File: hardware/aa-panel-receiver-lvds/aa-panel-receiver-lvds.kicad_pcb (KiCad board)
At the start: 2 copper layers, 95.4 x 54 mm, 44 parts, among them CN101 Conn_01x02, CN201 8P8C, CN202 Conn_01x08, CN251 Conn_01x04, U201 MC3486N, U202 Si8640EB-B-IU, U4 CRE1S0505S3C

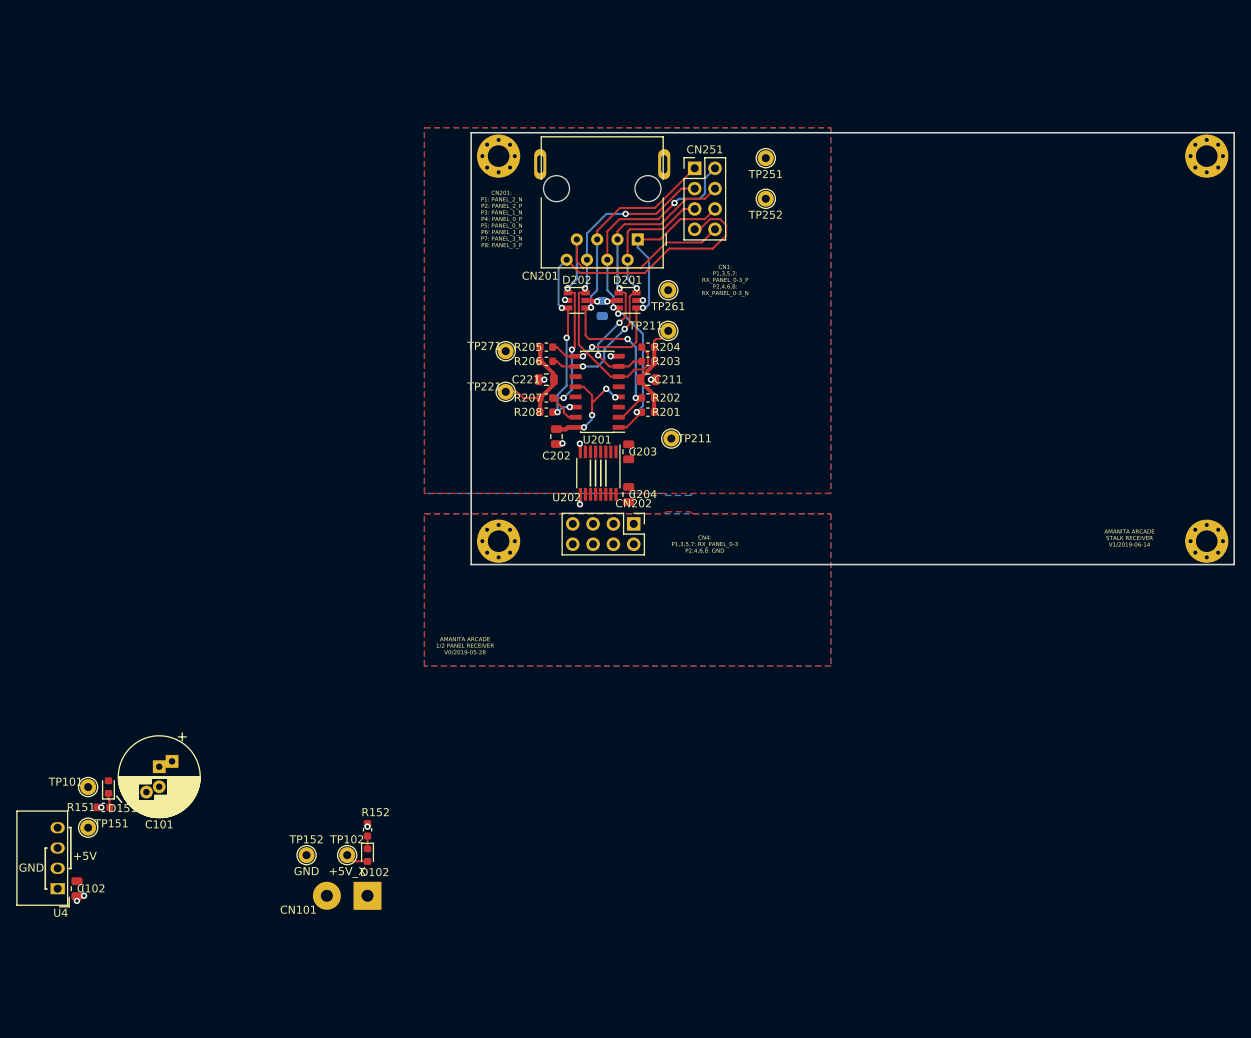
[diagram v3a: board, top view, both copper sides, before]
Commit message: Renumber and duplicate layout for panel receiver -- layout not complete
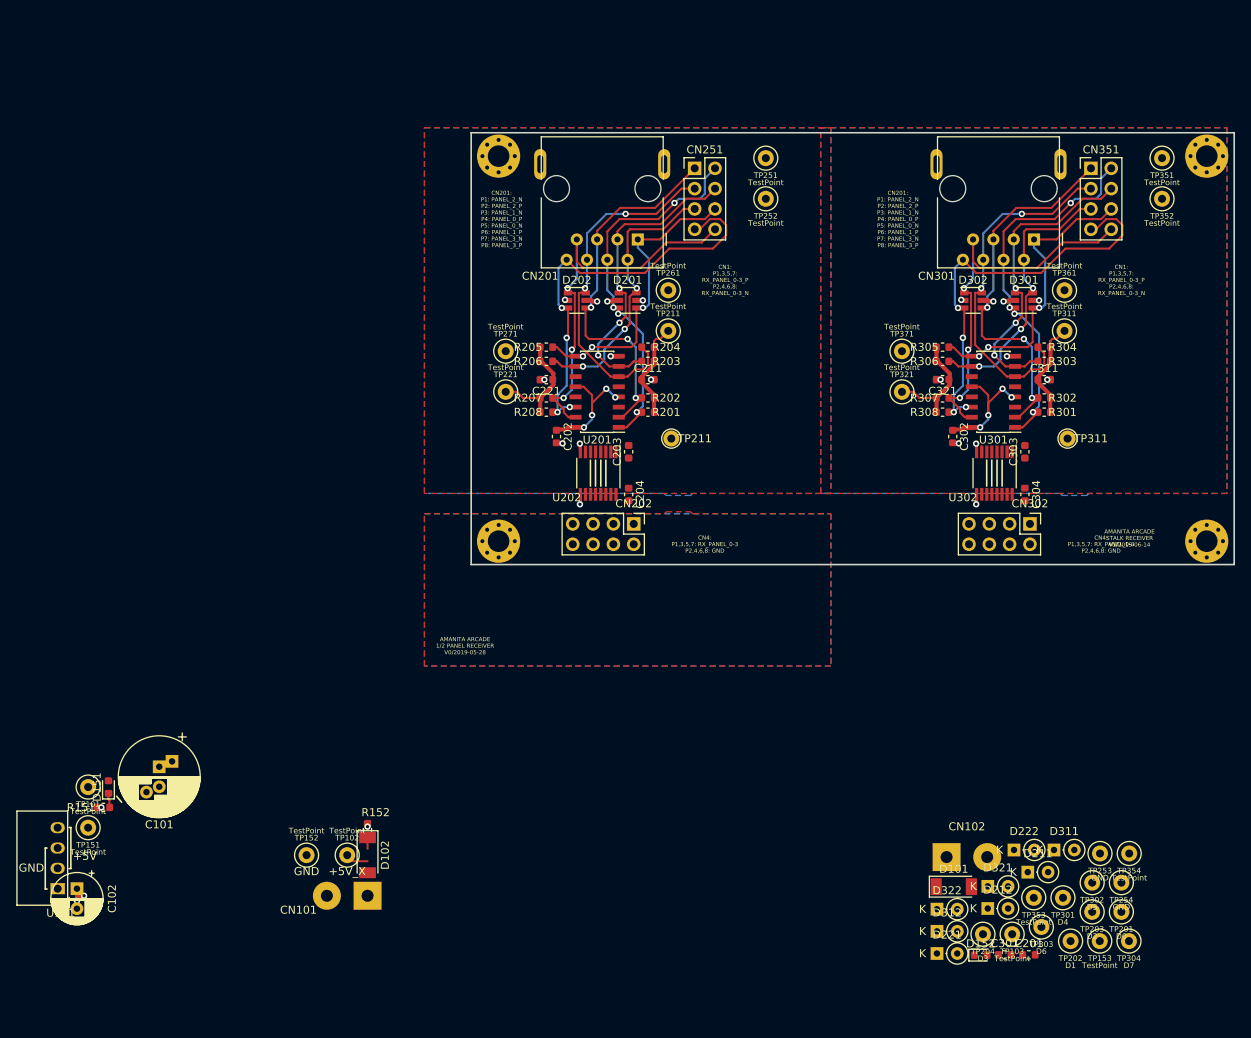
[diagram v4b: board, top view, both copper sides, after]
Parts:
- removed C1: 1u, Capacitor_SMD:C_0805_2012Metric
- added C201: 1u, Capacitor_SMD:C_0603_1608Metric, F.Cu at (161.2, 152.9)
- added C301: 1u, Capacitor_SMD:C_0603_1608Metric, F.Cu at (158.1, 152.9)
- added C302: 0.1u, Capacitor_SMD:C_0603_1608Metric, F.Cu at (151.6, 88.1)
- added C303: 0.1u, Capacitor_SMD:C_0603_1608Metric, F.Cu at (160.7, 90.0)
- added C304: 0.1u, Capacitor_SMD:C_0603_1608Metric, F.Cu at (160.7, 95.4)
- added C311: 0.1u, Capacitor_SMD:C_0603_1608Metric, F.Cu at (163.1, 81.0)
- added C321: 0.1u, Capacitor_SMD:C_0603_1608Metric, F.Cu at (150.4, 81.0)
- added CN102: Conn_01x02, Connector_Wire:SolderWirePad_1x02_P5.08mm_Drill1.5mm, F.Cu at (150.9, 140.7)
- added CN301: 8P8C, aa-shared:8P8C_Assmann_A-2014-2S-4, F.Cu at (161.8, 63.5)
- added CN302: Conn_01x08, Connector_PinHeader_2.54mm:PinHeader_2x04_P2.54mm_Vertical, F.Cu at (161.3, 99.1)
- added CN351: Conn_01x08, Connector_PinHeader_2.54mm:PinHeader_2x04_P2.54mm_Vertical, F.Cu at (168.9, 54.6)
- added D101: TSS83L45, aa-shared:D_SOD-128, F.Cu at (151.8, 144.4)
- added D152: LED, LED_SMD:LED_0603_1608Metric, F.Cu at (155.1, 153.0)
- added D211: D_Zener, Diode_THT:D_DO-35_SOD27_P2.54mm_Vertical_KathodeUp, F.Cu at (161.0, 142.6)
- added D212: D_Zener, Diode_THT:D_DO-35_SOD27_P2.54mm_Vertical_KathodeUp, F.Cu at (156.0, 147.1)
- added D221: D_Zener, Diode_THT:D_DO-35_SOD27_P2.54mm_Vertical_KathodeUp, F.Cu at (149.7, 152.8)
- added D222: D_Zener, Diode_THT:D_DO-35_SOD27_P2.54mm_Vertical_KathodeUp, F.Cu at (159.3, 139.8)
- added D301: D5V0P4UR6SO, Package_TO_SOT_SMD:SOT-23-6, F.Cu at (160.5, 71.1)
- added D302: D5V0P4UR6SO, Package_TO_SOT_SMD:SOT-23-6, F.Cu at (154.2, 71.1)
- added D311: D_Zener, Diode_THT:D_DO-35_SOD27_P2.54mm_Vertical_KathodeUp, F.Cu at (164.3, 139.8)
- added D312: D_Zener, Diode_THT:D_DO-35_SOD27_P2.54mm_Vertical_KathodeUp, F.Cu at (149.7, 150.0)
- added D321: D_Zener, Diode_THT:D_DO-35_SOD27_P2.54mm_Vertical_KathodeUp, F.Cu at (156.0, 144.4)
- added D322: D_Zener, Diode_THT:D_DO-35_SOD27_P2.54mm_Vertical_KathodeUp, F.Cu at (149.7, 147.2)
- added R301: 56, Resistor_SMD:R_0603_1608Metric, F.Cu at (163.1, 85.1)
- added R302: 56, Resistor_SMD:R_0603_1608Metric, F.Cu at (163.1, 83.3)
- added R303: 56, Resistor_SMD:R_0603_1608Metric, F.Cu at (163.1, 78.7)
- added R304: 56, Resistor_SMD:R_0603_1608Metric, F.Cu at (163.1, 77.0)
- added R305: 56, Resistor_SMD:R_0603_1608Metric, F.Cu at (150.4, 77.0)
- added R306: 56, Resistor_SMD:R_0603_1608Metric, F.Cu at (150.4, 78.7)
- added R307: 56, Resistor_SMD:R_0603_1608Metric, F.Cu at (150.4, 83.3)
- added R308: 56, Resistor_SMD:R_0603_1608Metric, F.Cu at (150.4, 85.1)
- added TP103: TestPoint, aa-shared:TestPoint_Loop_D1.80mm_Drill1.0mm_Beaded, F.Cu at (159.1, 150.3)
- added TP153: TestPoint, aa-shared:TestPoint_Loop_D1.80mm_Drill1.0mm_Beaded, F.Cu at (170.0, 151.2)
- added TP201: D0, aa-shared:TestPoint_Loop_D1.80mm_Drill1.0mm_Beaded, F.Cu at (172.7, 147.6)
- added TP202: D1, aa-shared:TestPoint_Loop_D1.80mm_Drill1.0mm_Beaded, F.Cu at (166.4, 151.2)
- added TP203: D2, aa-shared:TestPoint_Loop_D1.80mm_Drill1.0mm_Beaded, F.Cu at (169.1, 147.6)
- added TP204: D3, aa-shared:TestPoint_Loop_D1.80mm_Drill1.0mm_Beaded, F.Cu at (155.4, 150.3)
- added TP253: GND, aa-shared:TestPoint_Loop_D1.80mm_Drill1.0mm_Beaded, F.Cu at (170.0, 140.3)
- added TP254: GND, aa-shared:TestPoint_Loop_D1.80mm_Drill1.0mm_Beaded, F.Cu at (172.7, 143.9)
- added TP301: D4, aa-shared:TestPoint_Loop_D1.80mm_Drill1.0mm_Beaded, F.Cu at (165.4, 145.8)
- added TP302: D5, aa-shared:TestPoint_Loop_D1.80mm_Drill1.0mm_Beaded, F.Cu at (169.1, 143.9)
- added TP303: D6, aa-shared:TestPoint_Loop_D1.80mm_Drill1.0mm_Beaded, F.Cu at (162.7, 149.4)
- added TP304: D7, aa-shared:TestPoint_Loop_D1.80mm_Drill1.0mm_Beaded, F.Cu at (173.7, 151.2)
- added TP311: TestPoint, aa-shared:TestPoint_Loop_D1.80mm_Drill1.0mm_Beaded, F.Cu at (165.6, 74.9)
- added TP311: TestPoint, TestPoint:TestPoint_THTPad_D2.0mm_Drill1.0mm, F.Cu at (166.0, 88.4)
- added TP321: TestPoint, aa-shared:TestPoint_Loop_D1.80mm_Drill1.0mm_Beaded, F.Cu at (145.3, 82.5)
- added TP351: TestPoint, aa-shared:TestPoint_Loop_D1.80mm_Drill1.0mm_Beaded, F.Cu at (177.8, 53.3)
- added TP352: TestPoint, aa-shared:TestPoint_Loop_D1.80mm_Drill1.0mm_Beaded, F.Cu at (177.8, 58.4)
- added TP353: TestPoint, aa-shared:TestPoint_Loop_D1.80mm_Drill1.0mm_Beaded, F.Cu at (161.8, 145.8)
- added TP354: TestPoint, aa-shared:TestPoint_Loop_D1.80mm_Drill1.0mm_Beaded, F.Cu at (173.7, 140.3)
- added TP361: TestPoint, aa-shared:TestPoint_Loop_D1.80mm_Drill1.0mm_Beaded, F.Cu at (165.6, 69.8)
- added TP371: TestPoint, aa-shared:TestPoint_Loop_D1.80mm_Drill1.0mm_Beaded, F.Cu at (145.3, 77.5)
- added U301: ST26C32, Package_SO:SOIC-16_3.9x9.9mm_P1.27mm, F.Cu at (156.7, 82.5)
- added U302: Si8640EB-B-IU, Package_SO:QSOP-16_3.9x4.9mm_P0.635mm, F.Cu at (156.8, 92.7)
- C102: footprint Capacitor_SMD:C_0805_2012Metric -> Capacitor_THT:CP_Radial_D6.3mm_P2.50mm
- C202, C203, C204, C211, C221: footprint Capacitor_SMD:C_0805_2012Metric -> Capacitor_SMD:C_0603_1608Metric
- CN251: value Conn_01x04 -> Conn_01x08
- D102: value LED -> TSS83L45; footprint Diode_SMD:D_0603_1608Metric -> aa-shared:D_SOD-128
- D151: footprint Diode_SMD:D_0603_1608Metric -> LED_SMD:LED_0603_1608Metric
- TP101, TP102, TP151, TP152, TP211, TP221, TP251, TP252, TP261, TP271: footprint TestPoint:TestPoint_THTPad_D2.0mm_Drill1.0mm -> aa-shared:TestPoint_Loop_D1.80mm_Drill1.0mm_Beaded
- U201: value MC3486N -> ST26C32
- renumbered U4 to U101
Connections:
- net /IN_TX_PANEL_0 renamed /PANEL_0_S
- net /IN_TX_PANEL_0_N renamed /PANEL_0_N
- net /IN_TX_PANEL_0_P renamed /PANEL_0_P
- net /IN_TX_PANEL_1 renamed /PANEL_1_S
- net /IN_TX_PANEL_1_N renamed /PANEL_1_N
- net /IN_TX_PANEL_1_P renamed /PANEL_1_P
- net /IN_TX_PANEL_2 renamed /PANEL_2_S
- net /IN_TX_PANEL_2_N renamed /PANEL_2_N
- net /IN_TX_PANEL_2_P renamed /PANEL_2_P
- net /IN_TX_PANEL_3 renamed /PANEL_3_S
- net /IN_TX_PANEL_3_N renamed /PANEL_3_N
- net /IN_TX_PANEL_3_P renamed /PANEL_3_P
- net /TX_PANEL_0 renamed /PANEL_0
- net /TX_PANEL_1 renamed /PANEL_1
- net /TX_PANEL_2 renamed /PANEL_2
- net /TX_PANEL_3 renamed /PANEL_3
- C102 pad 1: +5V_X -> +5V
- D102 pad 1: Net-(D4-Pad1) -> +5V
- D102 pad 2: +5V_X -> +5V_Y
- H2 pad 1: GND -> GND_S
- H3 pad 1: GND_S -> GND
- R152 pad 1: Net-(D4-Pad1) -> Net-(D152-Pad1)
- U101 pad 2: +5V_X -> +5V
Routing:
- net /PANEL_7_P: track 0.00 -> 52.6 mm, vias 0 -> 4
- net /PANEL_7_N: track 0.00 -> 49.7 mm, vias 0 -> 3
- net /PANEL_4_N: track 0.00 -> 47.7 mm, vias 0 -> 4
- net /PANEL_4_P: track 0.00 -> 47.3 mm, vias 0 -> 3
- net /PANEL_5_P: track 0.00 -> 44.2 mm, vias 0 -> 2
- net /PANEL_5_N: track 0.00 -> 38.7 mm, vias 0 -> 3
- net /PANEL_6_N: track 0.00 -> 37.9 mm, vias 0 -> 3
- net /PANEL_6_P: track 0.00 -> 34.9 mm, vias 0 -> 3
- net +5V_SX: track 21.9 -> 42.0 mm, vias 6 -> 12
- net /+2.5B: track 14.3 -> 28.5 mm
- net /+2.5A: track 12.6 -> 25.1 mm
- net GND_S: track 5.84 -> 11.1 mm, vias 8 -> 15
- net GND: track 3.16 -> 4.42 mm, vias 4 -> 5

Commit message: Placement of components on panel receiver board, routing TBD
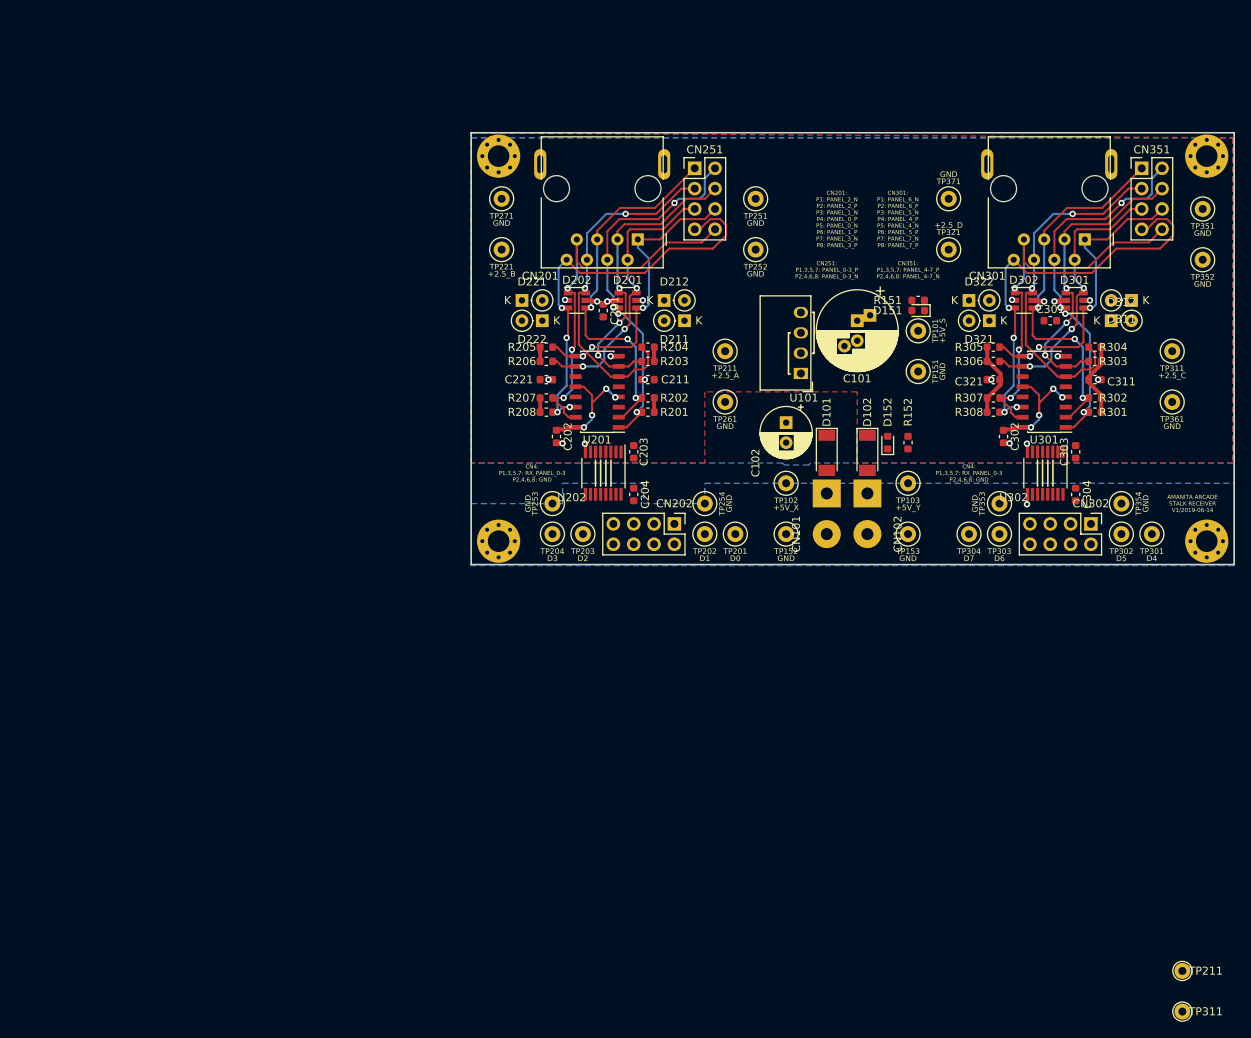
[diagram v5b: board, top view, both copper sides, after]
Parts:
- TP101: value TestPoint -> +5V_S
- TP102: value TestPoint -> +5V_X
- TP103: value TestPoint -> +5V_Y
- TP151, TP152, TP153, TP251, TP252, TP261, TP271, TP351, TP352, TP353, TP354, TP361, TP371: value TestPoint -> GND
- TP211: value TestPoint -> +2.5_A
- TP221: value TestPoint -> +2.5_B
- TP311: value TestPoint -> +2.5_C
- TP321: value TestPoint -> +2.5_D
- moved R151 120.0 mm to (147.3, 71.1)
- moved TP101 118.4 mm to (147.3, 74.9), turned to 90 degrees
- moved TP151 118.4 mm to (147.3, 80.0), turned to 90 degrees
- moved D151 117.4 mm to (147.3, 72.4), turned to 180 degrees
- moved U101 113.0 mm to (132.7, 80.3)
- moved C102 106.1 mm to (130.8, 86.4)
- moved C101 103.5 mm to (139.7, 73.7)
- moved D221 96.7 mm to (97.8, 71.1)
- moved C201 96.5 mm to (108.0, 72.4), turned to 270 degrees
- moved TP211 92.2 mm to (180.3, 154.9)
- moved D222 88.6 mm to (100.3, 73.7), turned to 180 degrees
- moved D212 86.1 mm to (115.6, 71.1)
- moved R152 83.1 mm to (146.1, 88.9)
- moved TP253 81.2 mm to (101.6, 96.5), turned to 270 degrees
- moved D211 81.2 mm to (118.1, 73.7), turned to 180 degrees
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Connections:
- net +5V_SX renamed +5V_S
- C311 pad 1: /+2.5A -> /+2.5C
- C321 pad 1: /+2.5B -> /+2.5D
- D311 pad 2: /+2.5A -> /+2.5C
- D312 pad 1: /+2.5A -> /+2.5C
- D321 pad 2: /+2.5B -> /+2.5D
- D322 pad 1: /+2.5B -> /+2.5D
- R301 pad 2: /+2.5A -> /+2.5C
- R302 pad 2: /+2.5A -> /+2.5C
- R303 pad 2: /+2.5A -> /+2.5C
- R304 pad 2: /+2.5A -> /+2.5C
- R305 pad 2: /+2.5B -> /+2.5D
- R306 pad 2: /+2.5B -> /+2.5D
- R307 pad 2: /+2.5B -> /+2.5D
- R308 pad 2: /+2.5B -> /+2.5D
- TP311 pad 1: /+2.5A -> /+2.5C
- TP321 pad 1: /+2.5B -> /+2.5D
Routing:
- net /+2.5B: track 28.5 -> 3.57 mm
- net /+2.5A: track 25.1 -> 3.57 mm
- net /+2.5D: track 0.00 -> 9.63 mm
- net /+2.5C: track 0.00 -> 9.51 mm
- net GND: track 4.42 -> 1.26 mm, vias 5 -> 1
- net +5V_X: track 2.86 -> 0.00 mm
- net +5V_S: track 42.0 -> 40.1 mm
- net Net-(D151-Pad1): track 1.81 -> 0.00 mm
- net Net-(D4-Pad1): track 1.63 -> 0.00 mm
- net GND_S: track 11.1 -> 10.6 mm, vias 15 -> 14
- removed copper zone on F.Cu, net +5V_X
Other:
- board text added: "4N"
- board text added: "4P"
- board text added: "5N"
- board text added: "5P"
- board text added: "6N"
- board text added: "6P"
- board text added: "7N"
- board text added: "7P"
- board text added: "CN251: P1,3,5,7: PANEL_0-3_P P2,4,6,8: PANEL_0-3_N"
- board text added: "CN301: P1: PANEL_6_N P2: PANEL_6_P P3: PANEL_5_N P4: PANEL_4_P P5: PANEL_4_N P6: PANEL_5_P P7: PANEL_7_N P8: PANEL_7_P"
- board text added: "CN351: P1,3,5,7: PANEL_4-7_P P2,4,6,8: PANEL_4-7_N"
- board text removed: "+5V"
- board text removed: "+5V_X"
- board text removed: "AMANITA ARCADE 1/2 PANEL RECEIVER V0/2019-05-28"
- board text removed: "CN1: P1,3,5,7: RX_PANEL_0-3_P P2,4,6,8: RX_PANEL_0-3_N"
- board text removed: "GND"

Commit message: Second rount almost ready, less fiducials
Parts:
- removed the TP211 at (180.3, 154.9)
- removed the TP311 at (180.3, 160.0)
- added TP104: +5V_Y, aa-shared:TestPoint_Loop_D1.80mm_Drill1.0mm_Beaded, F.Cu at (147.3, 94.0)
- TP102: value +5V_X -> +5V
- TP103: value +5V_Y -> +5V_X
- moved TP103 16.5 mm to (129.5, 94.0)
- moved TP102 15.3 mm to (144.8, 87.6), turned to 180 degrees
- moved D321 3.59 mm to (153.7, 71.1), turned to 0 degrees
- moved D322 3.59 mm to (156.2, 73.7), turned to 180 degrees
- moved R152 3.42 mm to (144.8, 92.1), turned to 180 degrees
- moved D211 2.54 mm to (118.1, 71.1)
- moved D212 2.54 mm to (115.6, 73.7)
- moved D152 1.80 mm to (144.8, 90.2), turned to 180 degrees
- moved TP151 1.80 mm to (148.6, 81.3), turned to 0 degrees
- moved U101 1.80 mm to (130.9, 80.0)
- moved C301 1.66 mm to (163.7, 72.0), turned to 270 degrees
- moved R151 1.42 mm to (148.6, 70.5)
- moved D151 1.27 mm to (148.6, 72.4)
- moved TP101 1.27 mm to (148.6, 74.9), turned to 0 degrees
- moved TP152 1.27 mm to (129.5, 100.3)
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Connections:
- TP102 pad 1: +5V_X -> +5V
- TP103 pad 1: +5V_Y -> +5V_X
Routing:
- net +5V_S: track 40.1 -> 16.0 mm, vias 12 -> 8
- net /+2.5A: track 3.57 -> 23.2 mm
- net /PANEL_0: track 0.00 -> 19.2 mm
- net /+2.5B: track 3.57 -> 22.6 mm
- net /PANEL_4: track 0.00 -> 15.9 mm
- net /PANEL_1: track 0.00 -> 15.3 mm
- net /+2.5C: track 9.51 -> 23.5 mm
- net /PANEL_2: track 0.00 -> 13.3 mm
- net /+2.5D: track 9.63 -> 22.6 mm
- net /PANEL_3: track 0.00 -> 12.8 mm
- net /PANEL_7: track 0.00 -> 12.2 mm
- net /PANEL_5: track 0.00 -> 12.1 mm
- net /PANEL_6: track 0.00 -> 11.0 mm
- net /PANEL_2_S: track 0.00 -> 10.9 mm, vias 0 -> 2
- net /PANEL_6_S: track 0.00 -> 10.4 mm, vias 0 -> 2
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- added copper zone on F.Cu, net +5V
- added copper zone on F.Cu, net +5V_X
- added copper zone on F.Cu, net +5V_Y
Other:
- board text added: "+5V"
- board text added: "AMANITA ARCADE STALK RECEIVER V1/2019-06-17"
- board text added: "CN202: P1,3,5,7: PANEL_0-3 P2,4,6,8: GND"
- board text added: "CN302: P1,3,5,7: PANEL_0-3 P2,4,6,8: GND"
- board text added: "GND"
- board text removed: "AMANITA ARCADE STALK RECEIVER V1/2019-06-14"
- board text removed: "CN4: P1,3,5,7: RX_PANEL_0-3 P2,4,6,8: GND"
